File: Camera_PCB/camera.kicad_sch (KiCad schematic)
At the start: 6 parts, among them J1 USB_B_Micro

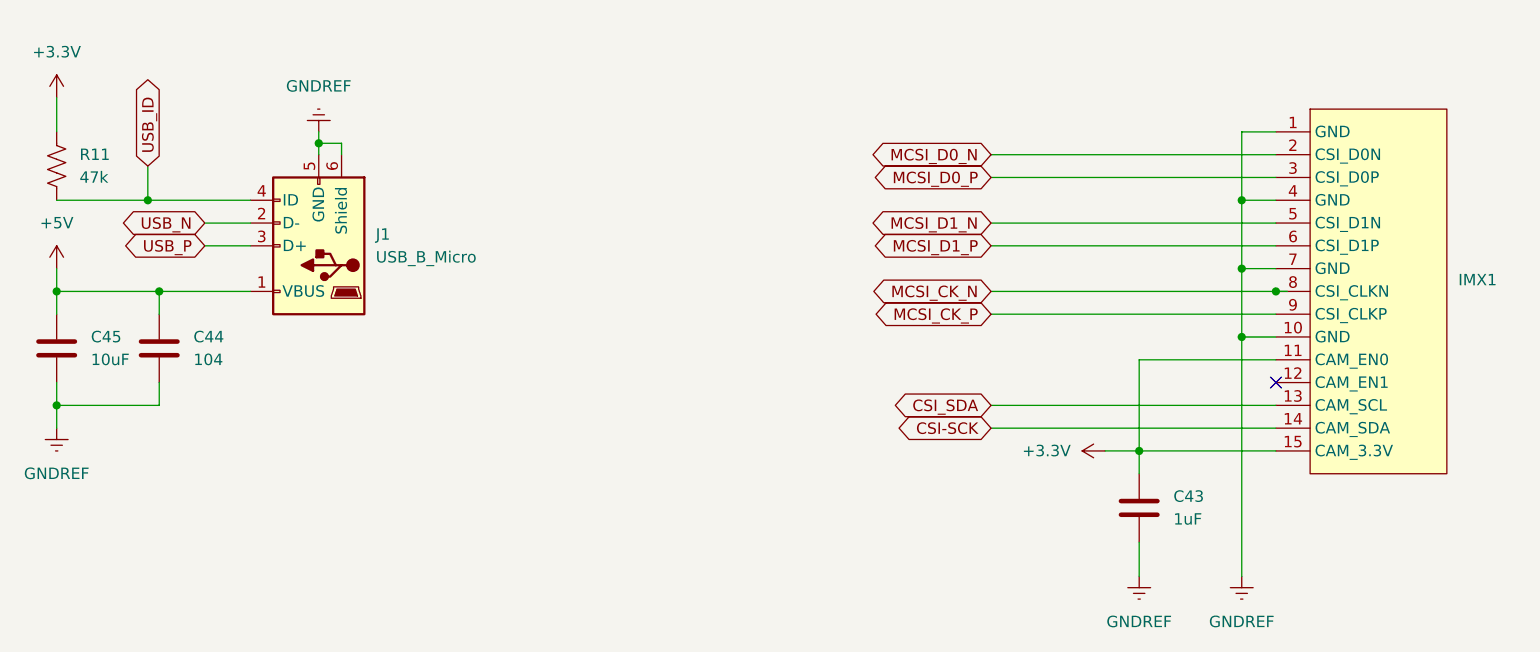
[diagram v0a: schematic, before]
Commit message: Readded Camera, USB connections
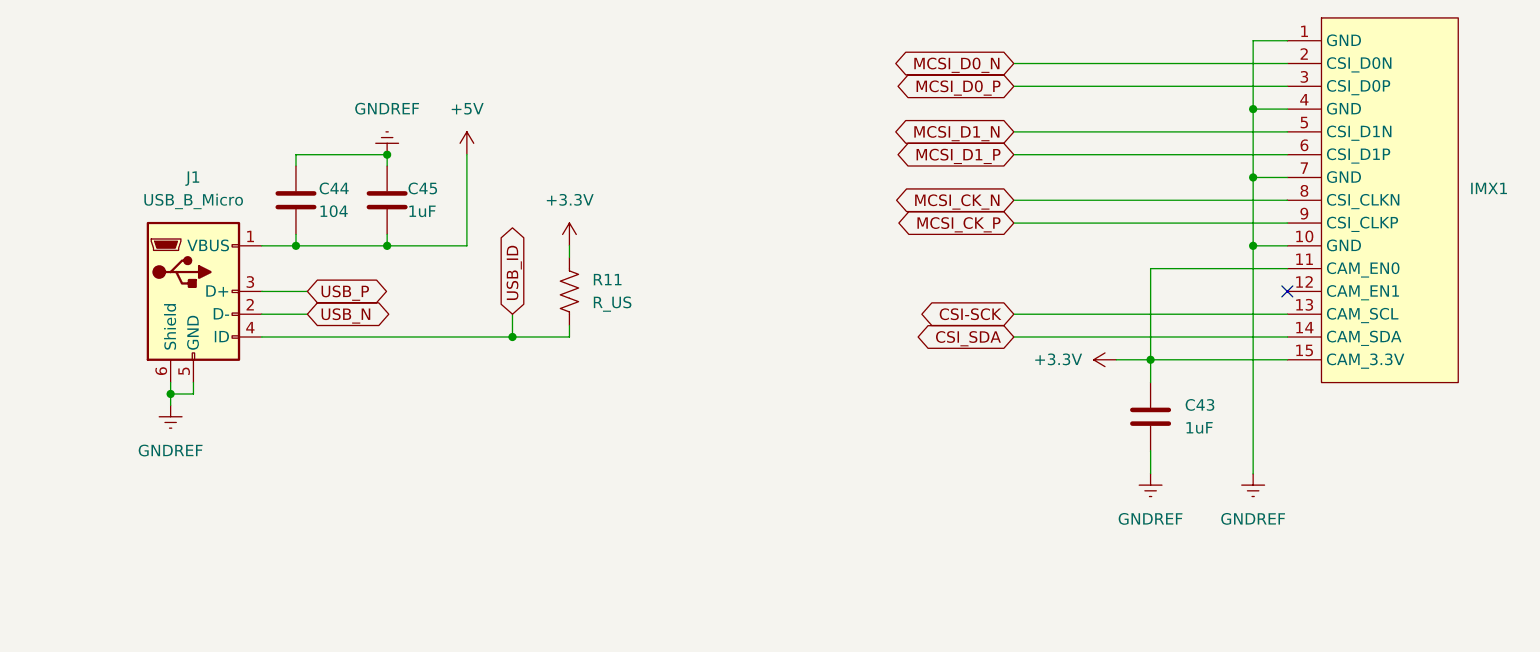
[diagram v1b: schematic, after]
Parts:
- C45: value 10uF -> 1uF
- R11: value 47k -> R_US
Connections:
- net +3.3V: now also R11.2; no longer R11.1
- net +5V: now also C44.2, C45.2; no longer C44.1, C45.1
- net CSI-SCK: now also IMX1.13 (CAM_SCL); no longer IMX1.14 (CAM_SDA)
- net CSI_SDA: now also IMX1.14 (CAM_SDA); no longer IMX1.13 (CAM_SCL)
- net GNDREF: now also C44.1, C45.1; no longer C44.2, C45.2
- net USB_ID: now also R11.1; no longer R11.2

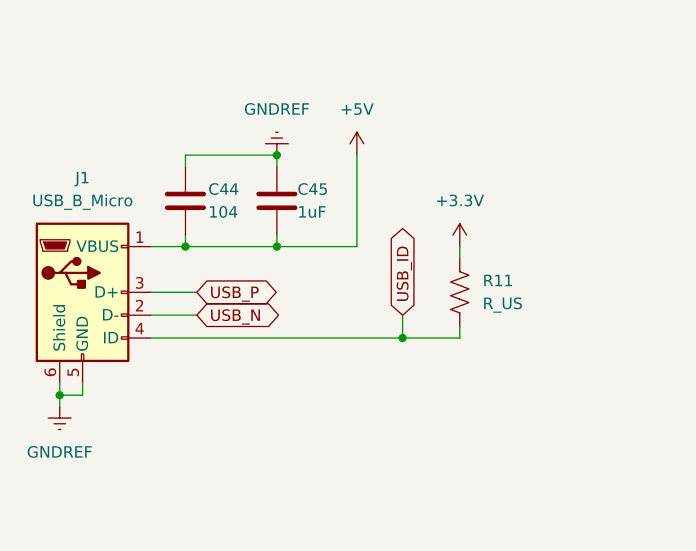
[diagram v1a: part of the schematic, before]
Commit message: Changed usb -> A 2.0
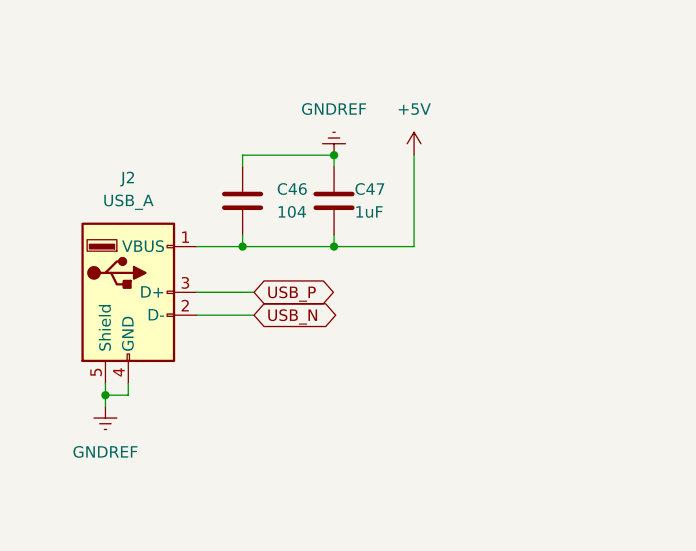
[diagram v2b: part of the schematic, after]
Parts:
- removed C44: 104, symbol Device:C
- removed C45: 1uF, symbol Device:C
- removed J1: USB_B_Micro, symbol Connector:USB_B_Micro
- removed R11: R_US, symbol Device:R_US
- added C46: 104, symbol Device:C
- added C47: 1uF, symbol Device:C
- added J2: USB_A, symbol Connector:USB_A
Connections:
- net +5V: now also C46.2, C47.2, J2.1 (VBUS)
- net GNDREF: now also C46.1, C47.1, J2.4 (GND), J2.5 (Shield)
- net USB_N: now also J2.2 (D-)
- net USB_P: now also J2.3 (D+)

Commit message: Switched pins 86, 87
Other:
- company: (none) -> Group 25 Senior Design
- title: (none) -> Wireless Backup Camera - Encoder
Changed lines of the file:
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@@
 	(generator_version "9.0")
 	(paper "A4")
+	(title_block
+		(title "Wireless Backup Camera - Encoder")
+		(company "Group 25 Senior Design")
+	)
 	(junction
 		(at 60.96 82.55)

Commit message: Started PCB
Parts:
- C43, C46, C47: footprint (none) -> Capacitor_SMD:C_0805_2012Metric_Pad1.18x1.45mm_HandSolder
- IMX1: footprint (none) -> Connector_FFC-FPC:TE_1-84952-5_1x15-1MP_P1.0mm_Horizontal
- J2: footprint (none) -> Connector_USB:USB_A_Connfly_DS1095
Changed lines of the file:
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@@
 			)
 		)
-		(property "Footprint" ""
+		(property "Footprint" "Connector_USB:USB_A_Connfly_DS1095"
 			(at 41.91 99.06 0)
 			(effects
@@
 			)
 		)
-		(property "Footprint" ""
+		(property "Footprint" "Capacitor_SMD:C_0805_2012Metric_Pad1.18x1.45mm_HandSolder"
 			(at 51.7652 91.44 0)
 			(effects
@@
 			)
 		)
-		(property "Footprint" ""
+		(property "Footprint" "Connector_FFC-FPC:TE_1-84952-5_1x15-1MP_P1.0mm_Horizontal"
 			(at 163.83 87.63 0)
 			(effects
@@
 			)
 		)
-		(property "Footprint" ""
+		(property "Footprint" "Capacitor_SMD:C_0805_2012Metric_Pad1.18x1.45mm_HandSolder"
 			(at 61.9252 91.44 0)
 			(effects
@@
 			)
 		)
-		(property "Footprint" ""
+		(property "Footprint" "Capacitor_SMD:C_0805_2012Metric_Pad1.18x1.45mm_HandSolder"
 			(at 140.6652 115.57 0)
 			(effects

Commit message: cleaned up PCB branch
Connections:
- net +5V: now also C46.1, C47.1; no longer C46.2, C47.2
- net GNDREF renamed GND
- net GND: now also C46.2, C47.2; no longer C46.1, C47.1
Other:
- moved on the sheet: C46, C47

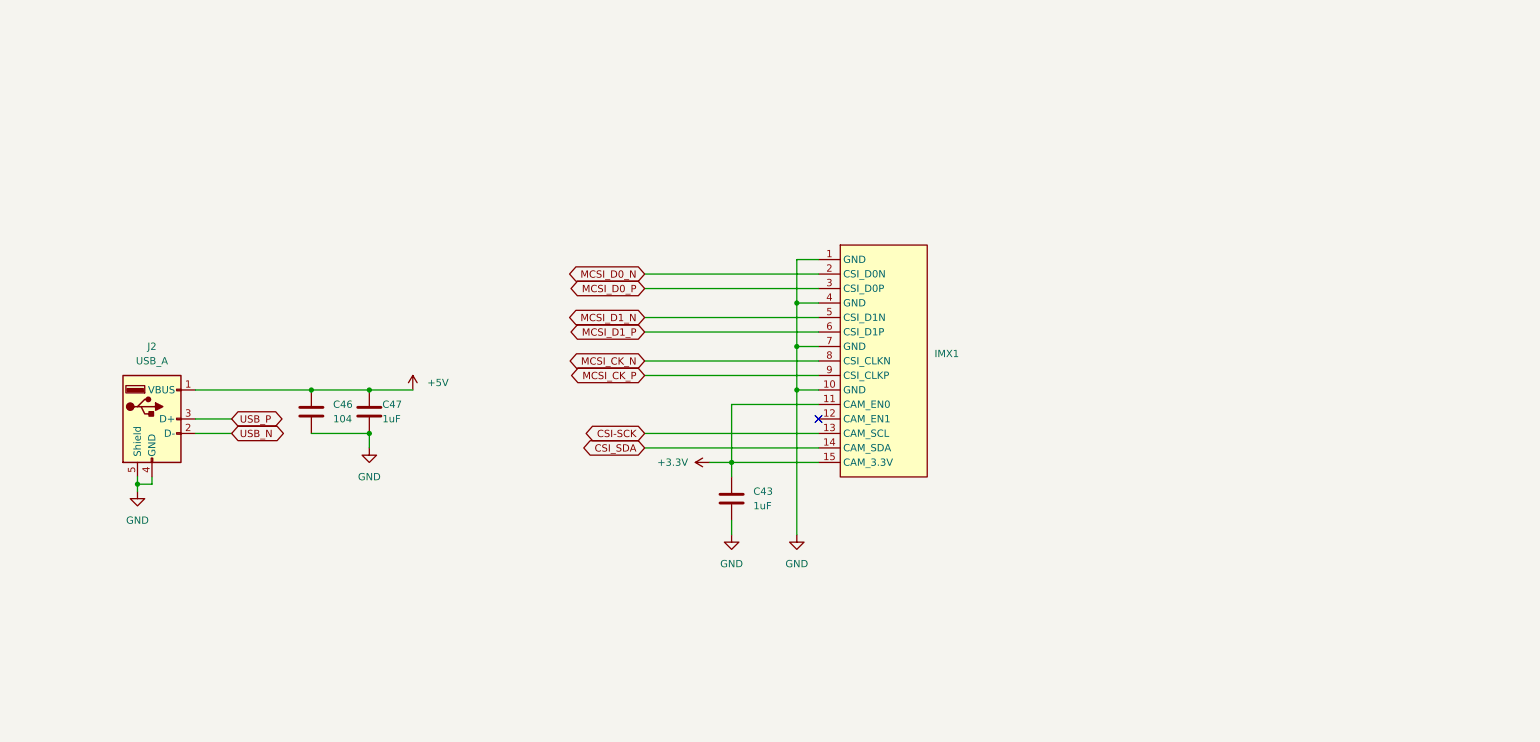
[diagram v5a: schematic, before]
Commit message: 10/29 Footprint Additions
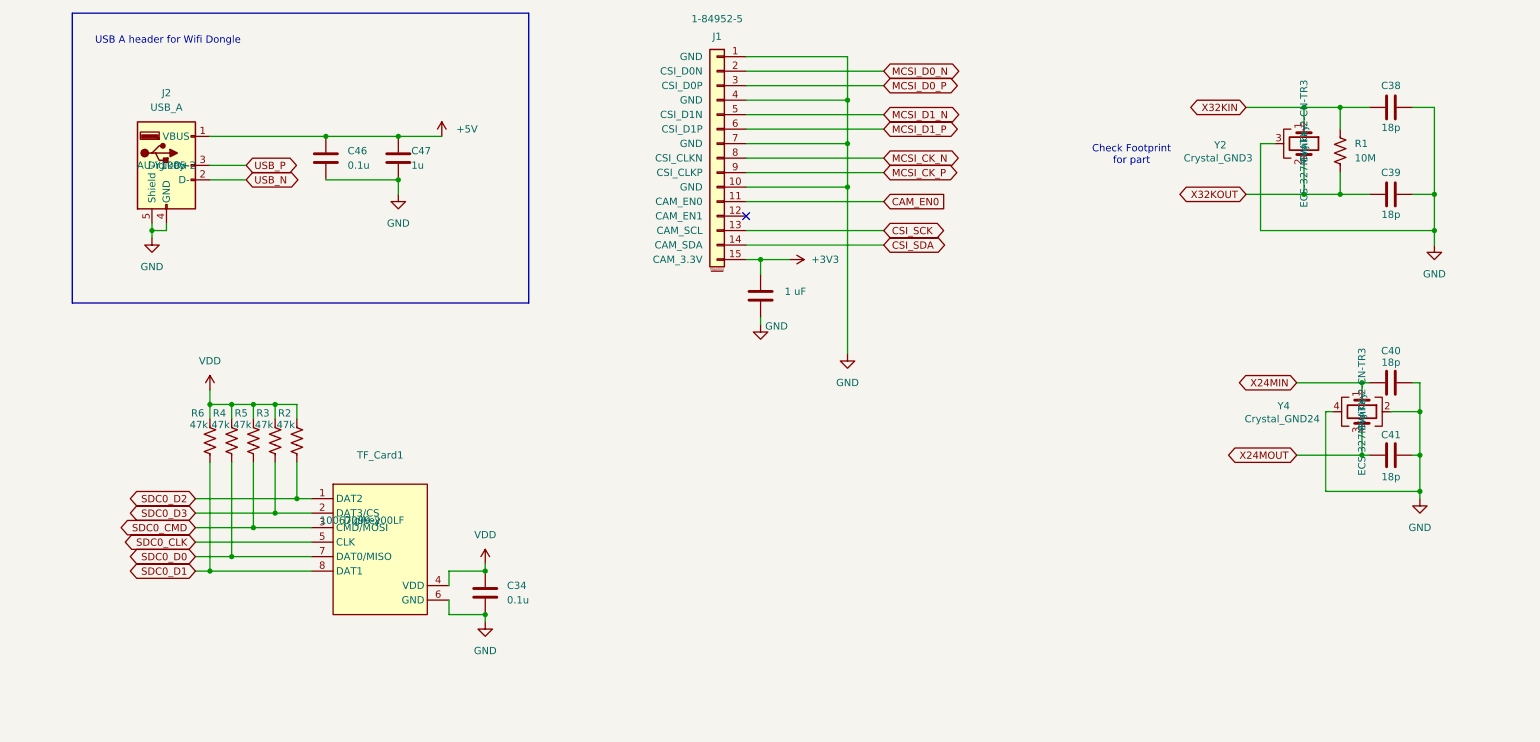
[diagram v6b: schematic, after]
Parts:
- removed C43: 1uF, Capacitor_SMD:C_0805_2012Metric_Pad1.18x1.45mm_HandSolder, symbol Device:C
- removed IMX1: ~, Connector_FFC-FPC:TE_1-84952-5_1x15-1MP_P1.0mm_Horizontal, symbol custom_chips:IMX219_Camera
- added C34: 0.1u, Capacitor_SMD:C_0603_1608Metric_Pad1.08x0.95mm_HandSolder, symbol Device:C
- added C38, C39, C40, C41: 18p, Capacitor_SMD:C_0603_1608Metric_Pad1.08x0.95mm_HandSolder, symbol Device:C
- added C4: 1 uF, Capacitor_SMD:C_0805_2012Metric_Pad1.18x1.45mm_HandSolder, symbol Device:C
- added J1: 1-84952-5, Connector_FFC-FPC:TE_1-84952-5_1x15-1MP_P1.0mm_Horizontal, symbol Connector_Generic_MountingPin:Conn_01x15_MountingPin_1
- added R1: 10M, Resistor_SMD:R_0805_2012Metric_Pad1.20x1.40mm_HandSolder, symbol Device:R_US
- added R2, R3, R4, R5, R6: 47k, Resistor_SMD:R_0805_2012Metric_Pad1.20x1.40mm_HandSolder, symbol Device:R_US
- added TF_Card1: ~, BackupCamCustomParts:AMPHENOL_10067099-200LF, symbol custom_chips:micro-sd-tf
- added Y2: Crystal_GND3, BackupCamCustomParts:OSC_ECS-2520S25-250-FN-TR, symbol Device:Crystal_GND3
- added Y4: Crystal_GND24, BackupCamCustomParts:OSC_ECS-2520S25-250-FN-TR, symbol Device:Crystal_GND24
- C46: value 104 -> 0.1u; footprint Capacitor_SMD:C_0805_2012Metric_Pad1.18x1.45mm_HandSolder -> Capacitor_SMD:C_0603_1608Metric_Pad1.08x0.95mm_HandSolder
- C47: value 1uF -> 1u
- J2: DPN (none) -> AU-Y1005-2; Distributor (none) -> Digikey
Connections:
- net CSI_SDA: now also J1.14 (CAM_SDA)
- net GND: now also C34.2, C38.2, C39.2, C4.2, C40.2, C41.1, J1.1 (GND), J1.10 (GND), J1.4 (GND), J1.7 (GND), TF_Card1.6 (GND), Y2.3, Y4.2, Y4.4
- net MCSI_CK_N: now also J1.8 (CSI_CLKN)
- net MCSI_CK_P: now also J1.9 (CSI_CLKP)
- net MCSI_D0_N: now also J1.2 (CSI_D0N)
- net MCSI_D0_P: now also J1.3 (CSI_D0P)
- net MCSI_D1_N: now also J1.5 (CSI_D1N)
- net MCSI_D1_P: now also J1.6 (CSI_D1P)
- new net +3V3: C4.1, J1.15 (CAM_3.3V)
- new net CAM_EN0: J1.11 (CAM_EN0)
- new net CSI_SCK: J1.13 (CAM_SCL)
- new net SDC0_CLK: TF_Card1.5 (CLK)
- new net SDC0_CMD: R5.2, TF_Card1.3 (CMD/MOSI)
- new net SDC0_D0: R4.2, TF_Card1.7 (DAT0/MISO)
- new net SDC0_D1: R6.2, TF_Card1.8 (DAT1)
- new net SDC0_D2: R2.2, TF_Card1.1 (DAT2)
- new net SDC0_D3: R3.2, TF_Card1.2 (DAT3/CS)
- new net VDD: C34.1, R2.1, R3.1, R4.1, R5.1, R6.1, TF_Card1.4 (VDD)
- new net X24MIN: C40.1, Y4.1
- new net X24MOUT: C41.2, Y4.3
- new net X32KIN: C38.1, R1.1, Y2.1
- new net X32KOUT: C39.1, R1.2, Y2.2
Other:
- note added: "Check Footprint for part"
- note added: "USB A header for Wifi Dongle"
- moved on the sheet: C46, C47, J2

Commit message: Camera PCB Schematic review 1
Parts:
- added J4: UART_0, Connector_PinHeader_2.54mm:PinHeader_1x03_P2.54mm_Vertical, symbol Connector:Conn_01x03_Pin
- added J5: UART_2, Connector_PinHeader_2.54mm:PinHeader_1x03_P2.54mm_Vertical, symbol Connector:Conn_01x03_Pin
- added R12, R13: 4.7k, Resistor_SMD:R_0805_2012Metric_Pad1.20x1.40mm_HandSolder, symbol Device:R_US
- J1: value 1-84952-5 -> MIPI-CSI2; DPN (none) -> 1-84952-5; Distributor (none) -> DigiKey
- J2: footprint Connector_USB:USB_A_Connfly_DS1095 -> Connector_USB:USB_A_Receptacle_GCT_USB1046; DPN AU-Y1005-2 -> USB1046-GF-0190-L-B-A; Distributor Digikey -> DigiKey
- J3: renamed from TF_Card1; value ~ -> SDA; Distributor Digikey -> DigiKey
- R1: footprint Resistor_SMD:R_0805_2012Metric_Pad1.20x1.40mm_HandSolder -> Resistor_SMD:R_0603_1608Metric_Pad0.98x0.95mm_HandSolder
- Y2: value Crystal_GND3 -> 32.768kHz XTAL; footprint BackupCamCustomParts:OSC_ECS-2520S25-250-FN-TR -> BackupCamCustomParts:XTAL_ECS-.327-12.5-38-TR; symbol Device:Crystal_GND3 -> Device:Crystal_GND23; DPN ECS-327MVATX-2-CN-TR3 -> ECS-.327-12.5-38-TR
- Y4: value Crystal_GND24 -> 24MHz XTAL; footprint BackupCamCustomParts:OSC_ECS-2520S25-250-FN-TR -> BackupCamCustomParts:XTAL_ECS-240-12-36-AGN-TR; DPN ECS-327MVATX-2-CN-TR3 -> ECS-240-12-36-AGN-TR
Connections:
- net +3V3: now also R12.1, R13.1
- net CSI_SCK: now also R12.2
- net CSI_SDA: now also R13.2
- net GND: now also J4.3 (Pin_3), J5.3 (Pin_3)
- net X32KOUT: now also Y2.4
- net VDD renamed +3.3V
- new net UART0_RX: J4.1 (Pin_1)
- new net UART0_TX: J4.2 (Pin_2)
- new net UART2_RX: J5.1 (Pin_1)
- new net UART2_TX: J5.2 (Pin_2)
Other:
- note added: "15-pin MIPI-CSI2 FPC Header"
- note added: "24MHz crystal"
- note added: "32.768kHz crystal"
- note added: "Hardware design guide reccomends leaving UART2 exposed"
- note added: "Specified by V3S: +/-40ppm Max ECS Datasheet: +/- 20ppm ECS datasheet says C_L=12.5pF, C_L=C/2+C_Stray Est. C_stray = 3pF -> C = 19pF, use 18pF"
- note added: "Specified by V3S: +/-40ppm Max ECS Datasheet: +/- 25ppm (tol) 30ppm (stab) ECS datasheet says C_L=12pF, C_L=C/2+C_Stray Est. C_stray = 3pF -> C = 18pF, use 18pF"
- note added: "TF/SD Card Slot"
- note added: "UART0 (System UART) UART2 (Backup UART)"
- note added: "Using 15 pin 1.0mm FPC connector with bottom contacts. Same pinout as raspberry pi cam"
- note added: "Using Raised 90 degree tf-card slot (similar to found on Licheepi zero) Not using Res. network because no 5-Res. networks"
- note removed: "Check Footprint for part"
- moved on the sheet: C34, C38, C39, C40, C41, C46, C47, J1, J2, J3, R1, R2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

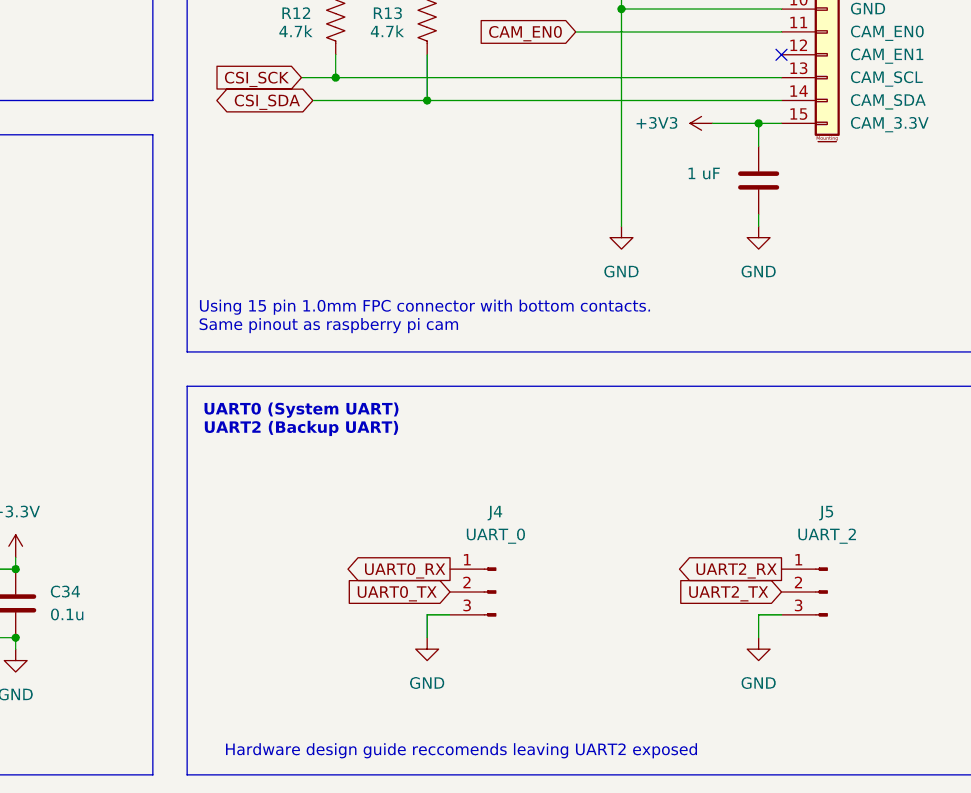
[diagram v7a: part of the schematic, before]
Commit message: Schematic done, thoroughly reviewed by Jack, should get reviewed by Connor if possible.
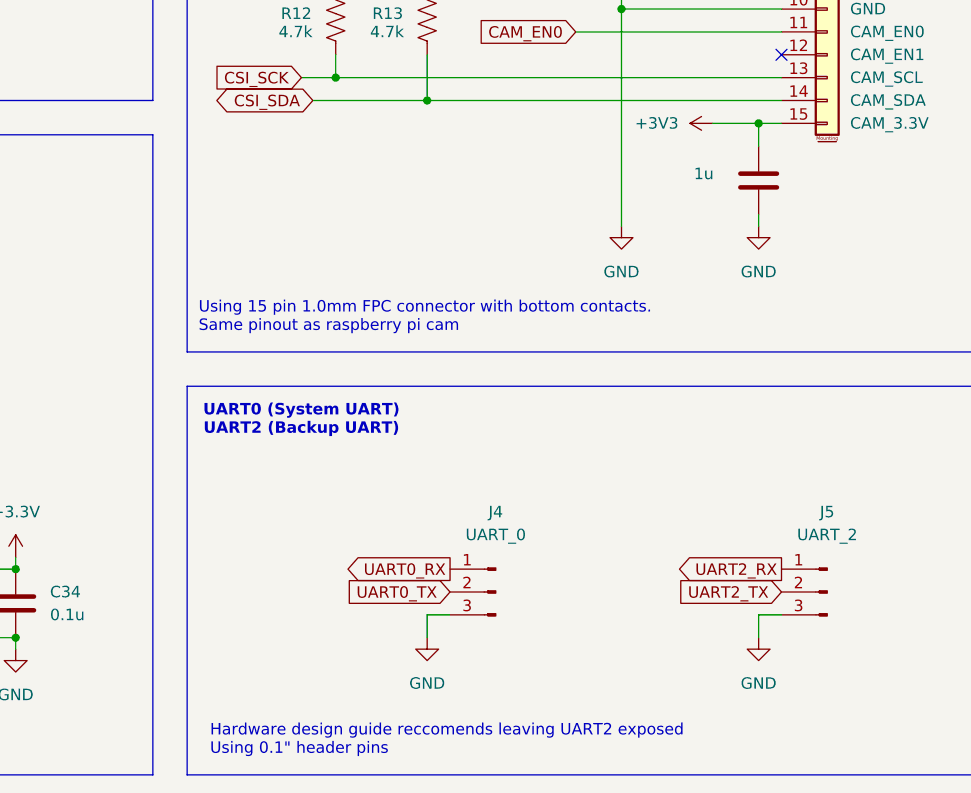
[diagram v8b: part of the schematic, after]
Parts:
- C34, C46: DPN (none) -> GRM188R72A104KA35D; Distributor (none) -> DigiKey
- C38, C39, C40, C41: DPN (none) -> GRM1885C1H180GA01D; Distributor (none) -> DigiKey
- C4: value 1 uF -> 1u; footprint Capacitor_SMD:C_0805_2012Metric_Pad1.18x1.45mm_HandSolder -> Capacitor_SMD:C_0603_1608Metric_Pad1.08x0.95mm_HandSolder; DPN (none) -> GCM188R71E105KA64D; Distributor (none) -> DigiKey
- C47: footprint Capacitor_SMD:C_0805_2012Metric_Pad1.18x1.45mm_HandSolder -> Capacitor_SMD:C_0603_1608Metric_Pad1.08x0.95mm_HandSolder; DPN (none) -> GCM188R71E105KA64D; Distributor (none) -> DigiKey
- J4, J5: Distributor (none) -> ECE Shop
- R1: DPN (none) -> RC0603FR-1010ML; Distributor (none) -> DigiKey
- R12, R13: footprint Resistor_SMD:R_0805_2012Metric_Pad1.20x1.40mm_HandSolder -> Resistor_SMD:R_0603_1608Metric_Pad0.98x0.95mm_HandSolder; DPN (none) -> RC0603FR-074K7L; Distributor (none) -> DigiKey
- R2, R3, R4, R5, R6: footprint Resistor_SMD:R_0805_2012Metric_Pad1.20x1.40mm_HandSolder -> Resistor_SMD:R_0603_1608Metric_Pad0.98x0.95mm_HandSolder; DPN (none) -> RC0603FR-0747KL; Distributor (none) -> DigiKey
- Y2: Distributor Digikey -> DigiKey
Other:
- note added: "Hardware design guide reccomends leaving UART2 exposed Using 0.1" header pins"
- note removed: "Hardware design guide reccomends leaving UART2 exposed"
